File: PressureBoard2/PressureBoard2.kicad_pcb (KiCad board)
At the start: 2 copper layers, 17 parts, among them J1 POWER_JACK, J2 Conn_01x02_Male, J3 Conn_01x02_Male, J4 Conn_01x02_Male, SW1 TL2230OA, U1 ASDXACX030PAAA5

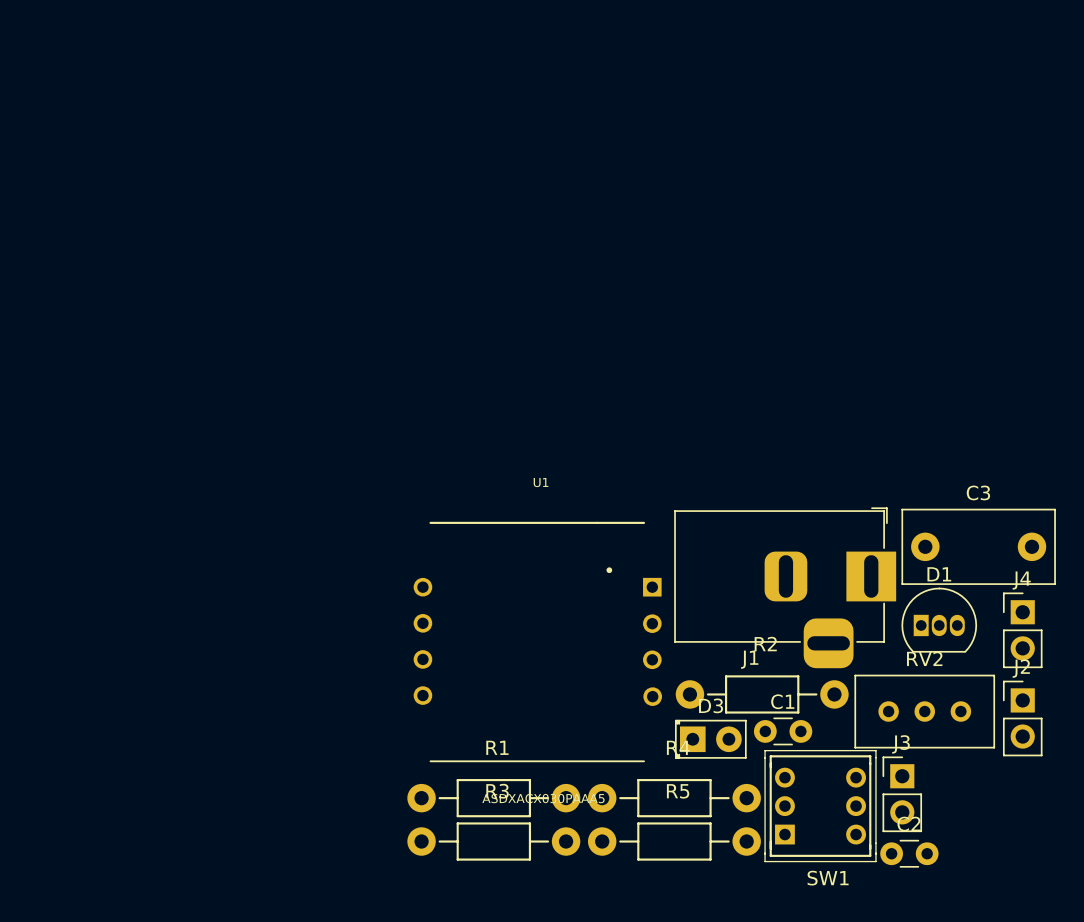
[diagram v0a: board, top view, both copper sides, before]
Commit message: PCVBV1
Agrego versión de PCB con ruteo y llenado de zonas de cobre.
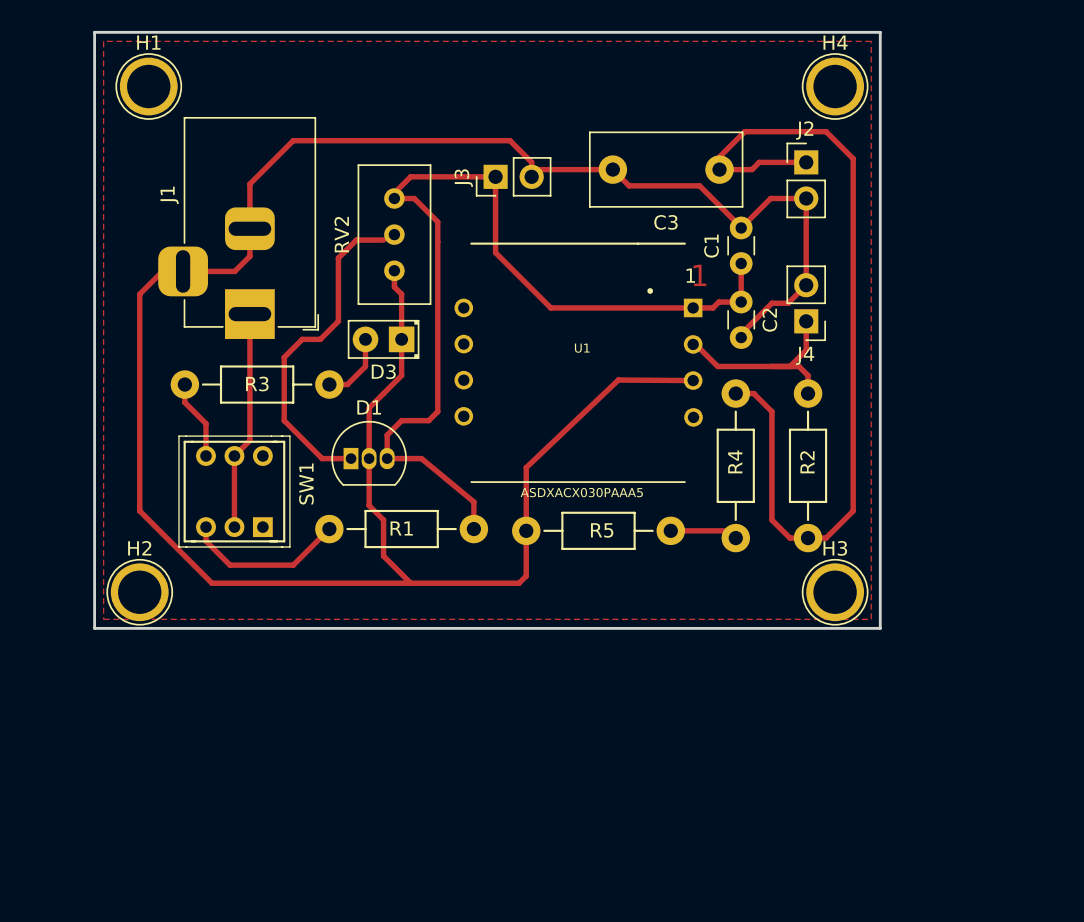
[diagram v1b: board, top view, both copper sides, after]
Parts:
- added H1: 1pin, Connect:1pin, F.Cu at (101.6, 69.8)
- added H2: 1pin, Connect:1pin, F.Cu at (101.0, 105.4)
- added H3: 1pin, Connect:1pin, F.Cu at (149.9, 105.4)
- added H4: 1pin, Connect:1pin, F.Cu at (149.9, 69.8)
- J1: value POWER_JACK -> Barrel_Jack_Switch
- R3: value 560 -> 1k
- moved RV2 53.7 mm to (118.9, 77.7), turned to 90 degrees
- moved J3 50.9 mm to (126.0, 76.2), turned to 90 degrees
- moved J1 47.4 mm to (108.7, 85.9), turned to 270 degrees
- moved SW1 42.8 mm to (111.1, 100.3), turned to 90 degrees
- moved D1 41.8 mm to (115.8, 96.0)
- moved J2 40.8 mm to (147.8, 75.2)
- moved C2 40.2 mm to (143.3, 85.0), turned to 270 degrees
- moved D3 34.8 mm to (119.4, 87.6), turned to 180 degrees
- moved C1 32.9 mm to (143.3, 82.3), turned to 90 degrees
- moved R3 32.8 mm to (114.3, 90.8), turned to 180 degrees
- moved C3 30.2 mm to (141.7, 75.7), turned to 180 degrees
- moved J4 25.5 mm to (147.8, 86.4), turned to 180 degrees
- moved R5 22.5 mm to (128.1, 101.1)
- moved R4 20.6 mm to (142.9, 101.6), turned to 90 degrees
- moved U1 19.8 mm to (132.1, 88.9)
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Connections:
- J1 pad 1: (no net) -> Net-(J1-Pad1)
- J1 pad 2: (no net) -> GND
- J1 pad 3: (no net) -> GND
- SW1 pad 2: Net-(J1-PadPWR) -> Net-(J1-Pad1)
- SW1 pad 5: Net-(J1-PadPWR) -> Net-(J1-Pad1)
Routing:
- net GND: track 0.00 -> 162.0 mm
- net VCC: track 0.00 -> 67.1 mm
- net Net-(C3-Pad1): track 0.00 -> 60.0 mm
- net Net-(D1-Pad1): track 0.00 -> 23.3 mm
- net Net-(J1-Pad1): track 0.00 -> 15.4 mm
- net Net-(J4-Pad1): track 0.00 -> 15.2 mm
- net Net-(R1-Pad2): track 0.00 -> 11.4 mm
- net Net-(R3-Pad2): track 0.00 -> 5.64 mm
- net Net-(D3-Pad2): track 0.00 -> 4.97 mm
- net Net-(R4-Pad1): track 0.00 -> 4.78 mm
- added copper zone on B.Cu, net GND
- added copper zone on F.Cu, net VCC
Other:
- board outline added: 55.2 x 41.9 mm
- net class PressureBoard added: clearance 0.2, trace_width 0.3048, via_dia 1.905, via_drill 0.3
- rule pad_to_mask_clearance: 0.051 -> 0
- board text added: "1"

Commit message: PCB_V3
Agrego correcciones en footprints del ASDX, Switch DPDT  y modificaciones en ruteo.
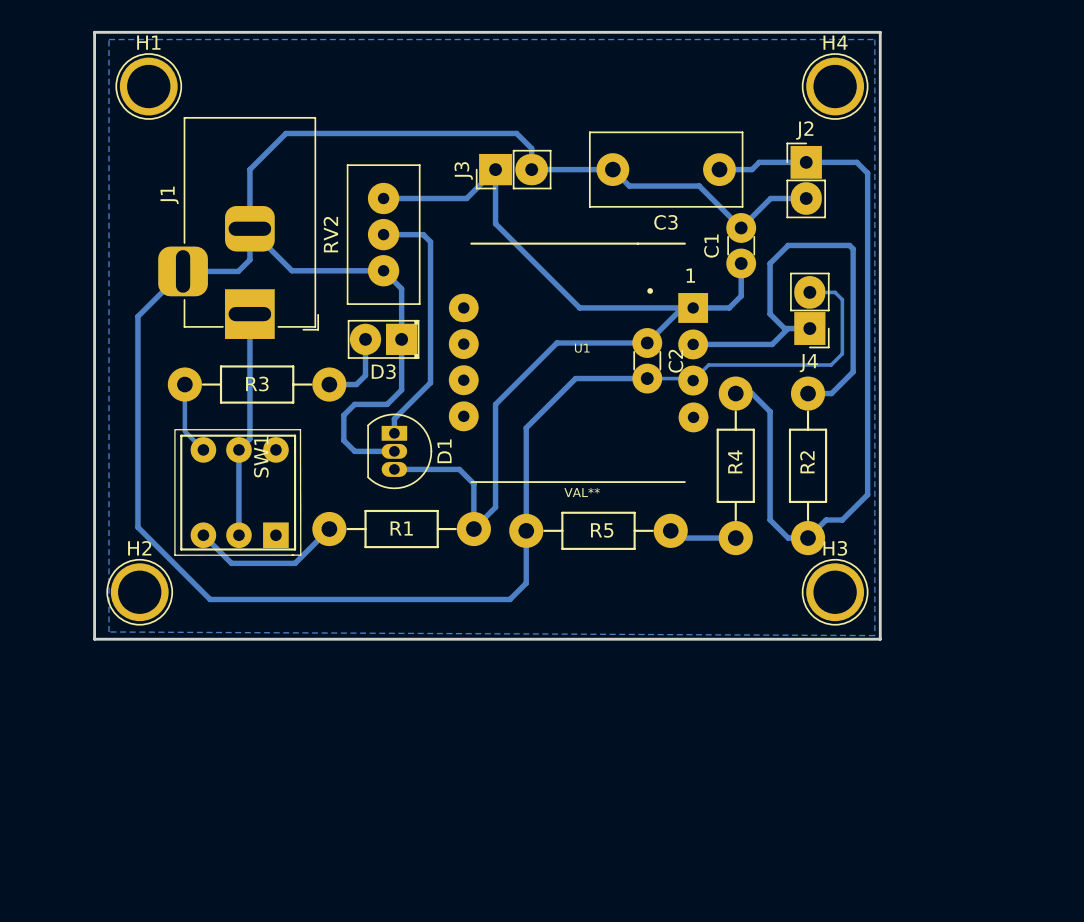
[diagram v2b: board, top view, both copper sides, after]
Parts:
- U1: value ASDXACX030PAAA5 -> VAL**
- moved C2 7.21 mm to (136.7, 87.9)
- moved SW1 3.70 mm to (108.0, 98.4)
- moved D1 3.53 mm to (118.9, 94.2), turned to 270 degrees
- moved RV2 0.76 mm to (118.1, 77.7)
- moved J4 0.57 mm to (148.1, 86.9)
- moved J3 0.51 mm to (126.0, 75.7)
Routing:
- net Net-(J4-Pad1): track 15.2 -> 32.8 mm
- net GND: track 162.0 -> 177.5 mm
- net Net-(C3-Pad1): track 60.0 -> 52.8 mm
- net Net-(D1-Pad1): track 23.3 -> 18.0 mm
- net VCC: track 67.1 -> 71.7 mm
- net Net-(R4-Pad1): track 4.78 -> 5.50 mm
- net Net-(R3-Pad2): track 5.64 -> 5.14 mm
- removed copper zone on F.Cu, net VCC
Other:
- board size 55.2 x 41.9 mm -> 55.2 x 42.7 mm
- net class PressureBoard: trace_width 0.3048 -> 0.3148

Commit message: Se mejoro el Layout
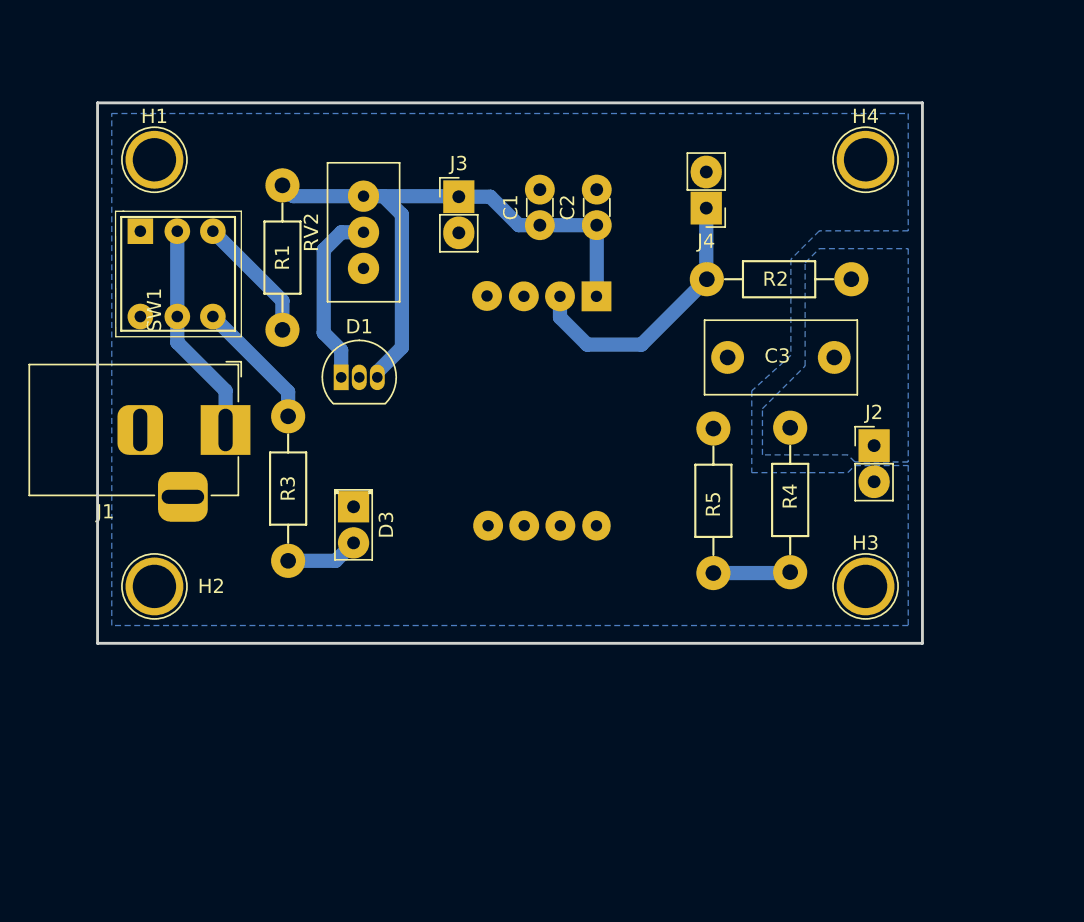
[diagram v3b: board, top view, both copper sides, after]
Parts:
- U1: moved to B.Cu
- moved R1 27.7 mm to (111.0, 76.8), turned to 270 degrees
- moved J2 20.5 mm to (152.6, 95.1)
- moved R2 18.5 mm to (151.0, 83.4), turned to 180 degrees
- moved SW1 16.0 mm to (103.6, 83.0), turned to 270 degrees
- moved C3 15.5 mm to (149.8, 88.9)
- moved R5 15.0 mm to (141.3, 93.9), turned to 270 degrees
- moved C1 14.4 mm to (129.1, 79.6)
- moved R3 12.7 mm to (111.4, 103.2), turned to 90 degrees
- moved D3 12.2 mm to (116.0, 99.4), turned to 270 degrees
- moved J4 11.2 mm to (140.8, 78.4)
- moved C2 9.01 mm to (133.1, 79.6), turned to 90 degrees
- moved J1 8.33 mm to (107.0, 94.0), turned to 0 degrees
- moved H4 5.58 mm to (152.0, 75.0)
- moved D1 5.43 mm to (115.1, 90.3), turned to 0 degrees
- moved H1 5.17 mm to (102.0, 75.0)
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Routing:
- net GND: track 177.5 -> 0.00 mm
- net Net-(C3-Pad1): track 52.8 -> 0.00 mm
- net VCC: track 71.7 -> 42.3 mm
- net Net-(J4-Pad1): track 32.8 -> 19.5 mm
- net Net-(D1-Pad1): track 18.0 -> 12.8 mm
- net Net-(R3-Pad2): track 5.14 -> 9.21 mm
- net Net-(R1-Pad2): track 11.7 -> 8.96 mm
- added copper zone on B.Cu, net Net-(C3-Pad1)
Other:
- board size 55.2 x 42.7 mm -> 58 x 38 mm
- net class Default: trace_width 0.25 -> 1
- net class PressureBoard: trace_width 0.3148 -> 0.381
- board text removed: "1"
